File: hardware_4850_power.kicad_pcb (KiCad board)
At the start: 4 copper layers, 84 x 79 mm, 88 parts, among them J103 PWM, J104 ADC, J105 +, J106 A, J107 B, J108 C, J109 GND, Q201 NCEP6080AG, Q202 NCEP6080AG, Q203 NCEP6080AG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

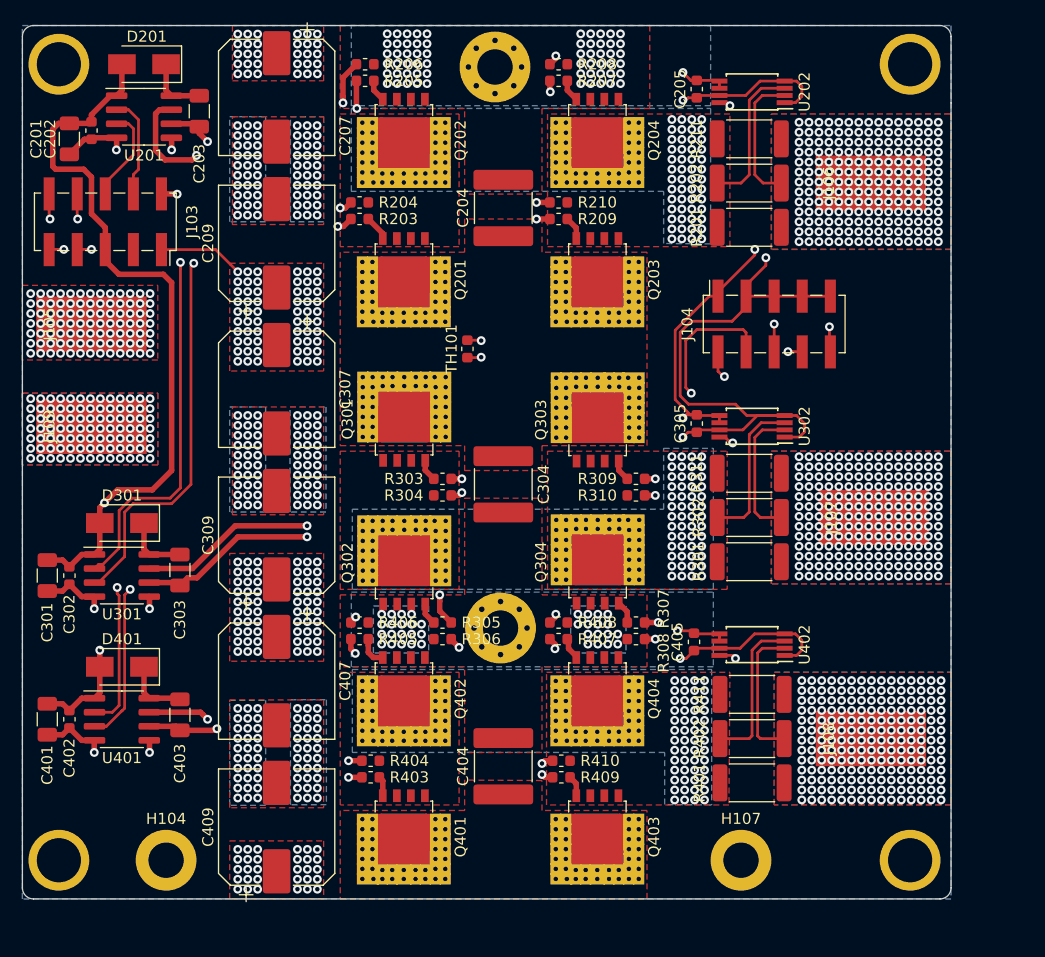
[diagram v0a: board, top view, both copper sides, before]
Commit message: Made gerbers ready to order
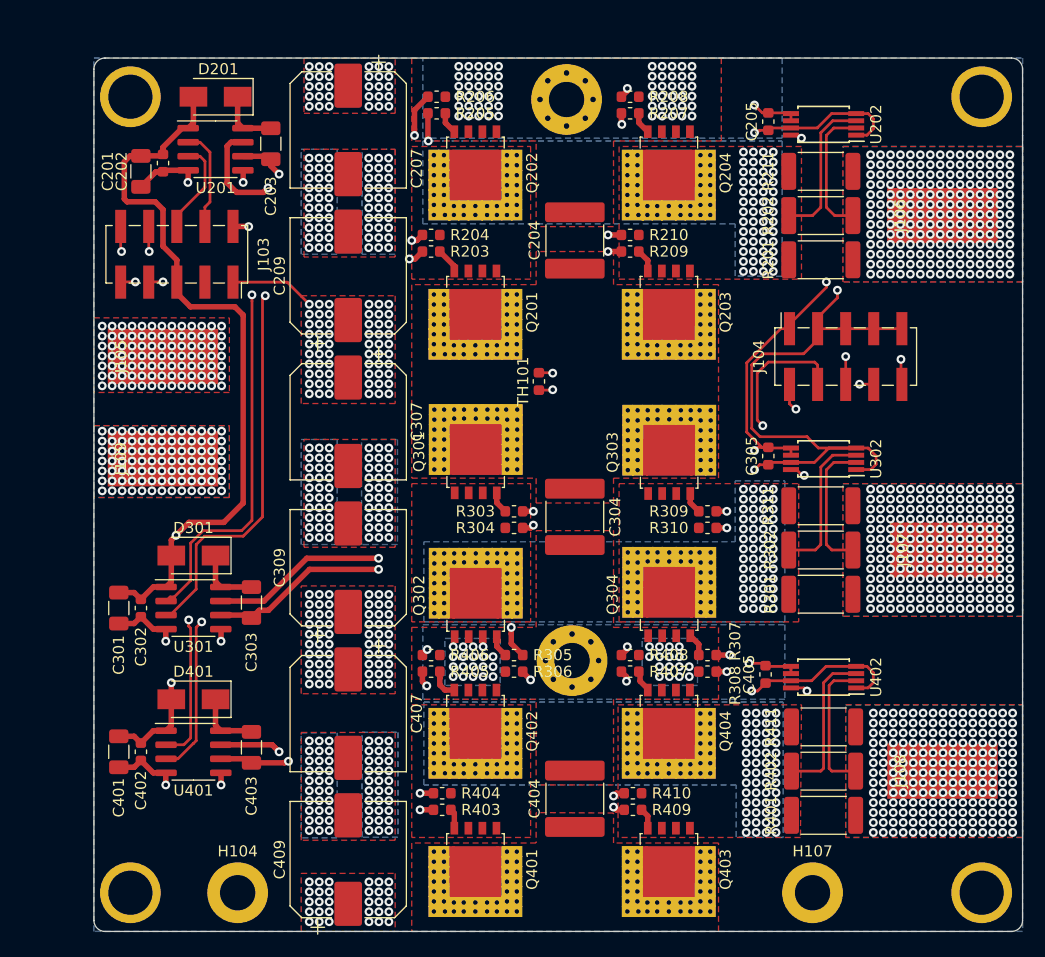
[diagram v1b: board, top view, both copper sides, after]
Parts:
- moved C309 7.11 mm to (121.2, 102.0)
- moved C403 7.11 mm to (112.5, 118.3)
- moved Q201 7.11 mm to (132.7, 78.0)
- moved Q203 7.11 mm to (150.2, 78.0)
- moved C201 7.11 mm to (102.5, 66.2)
- moved C202 7.11 mm to (104.5, 65.4)
- moved C203 7.11 mm to (114.2, 63.7)
- moved C204 7.11 mm to (141.7, 72.4)
- moved C205 7.11 mm to (159.2, 61.7)
- moved C207 7.11 mm to (121.2, 62.4)
- moved C209 7.11 mm to (121.2, 75.6)
- moved C301 7.11 mm to (100.5, 105.7)
- moved C302 7.11 mm to (102.5, 105.7)
- moved C303 7.11 mm to (112.5, 105.2)
- moved C304 7.11 mm to (141.7, 97.4)
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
